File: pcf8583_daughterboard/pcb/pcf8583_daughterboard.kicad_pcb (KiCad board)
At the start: 2 copper layers, 22.9 x 20.3 mm, 11 parts

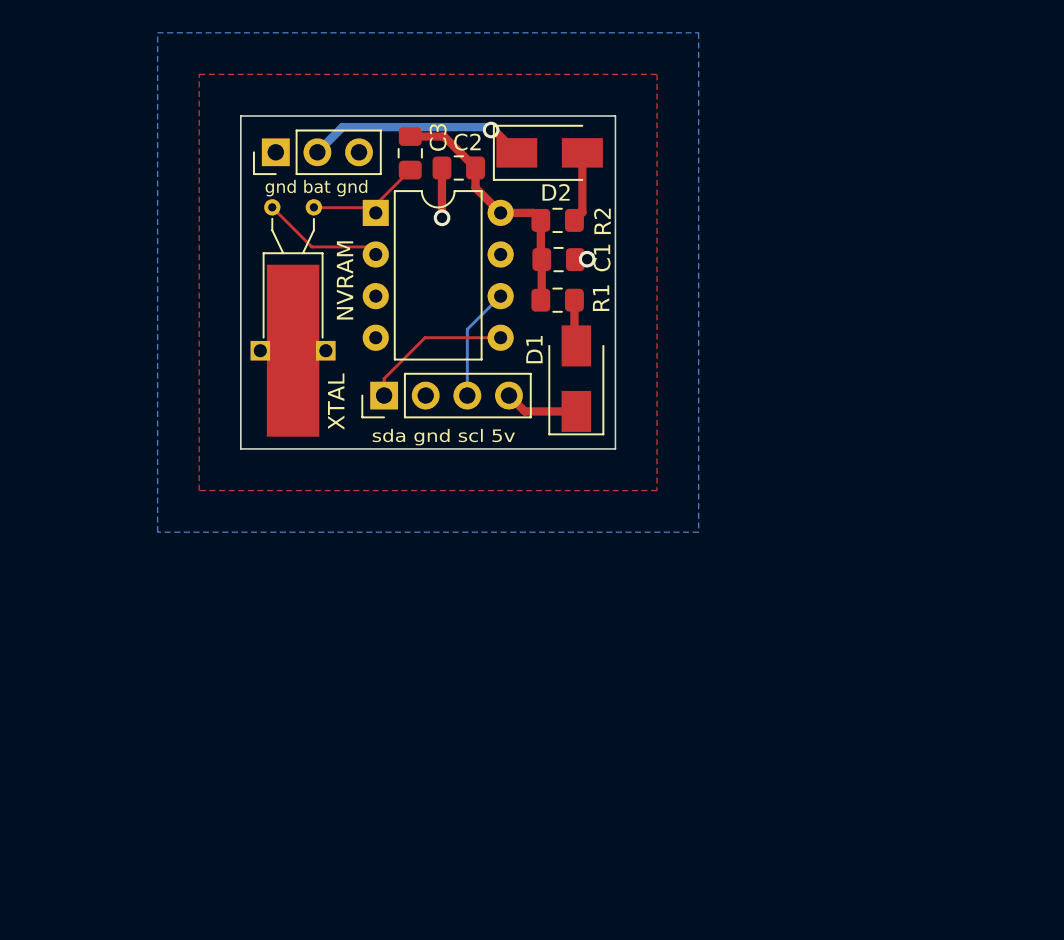
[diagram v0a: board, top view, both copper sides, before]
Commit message: Add supercap to pcf8583 daughterboard and make it a bit bigger, with mounting holes
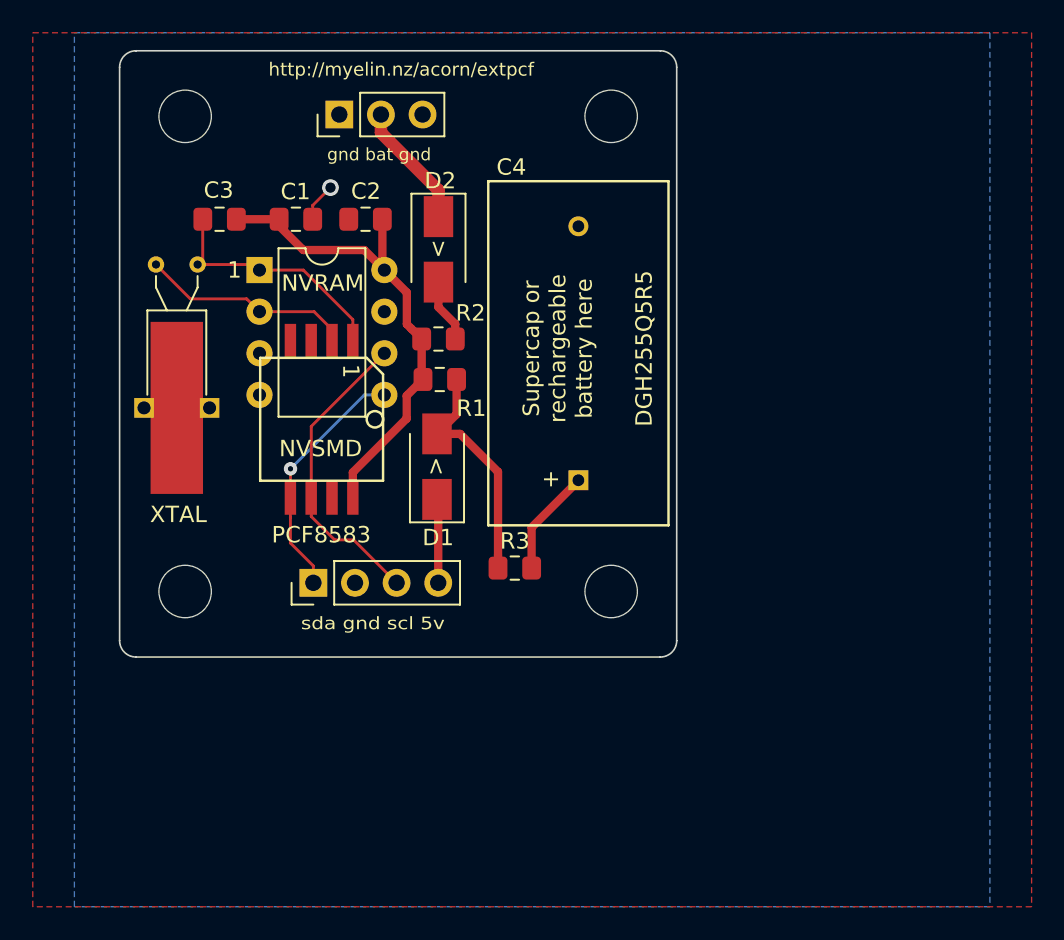
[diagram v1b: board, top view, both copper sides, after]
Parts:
- added C4: DGH255Q5R5, myelin-kicad:dgh255q5r5, F.Cu at (173.0, 108.5)
- added NVSMD: PCF8583, myelin-kicad:so8_pcf8583t_7.5x7.5mm, F.Cu at (157.3, 112.5)
- added R3: 180R, Resistor_SMD:R_0805_2012Metric_Pad1.15x1.40mm_HandSolder, F.Cu at (169.1, 121.6)
- added REF**: MountingHole_3.2mm_M3, MountingHole:MountingHole_3.2mm_M3, F.Cu at (149.0, 94.0)
- added REF**: MountingHole_3.2mm_M3, MountingHole:MountingHole_3.2mm_M3, F.Cu at (175.0, 94.0)
- added REF**: MountingHole_3.2mm_M3, MountingHole:MountingHole_3.2mm_M3, F.Cu at (175.0, 123.0)
- added REF**: MountingHole_3.2mm_M3, MountingHole:MountingHole_3.2mm_M3, F.Cu at (149.0, 123.0)
- NVRAM: value PCF8583P -> PCF8583
- R1, R2: value 100R -> 47R
- moved C1 16.2 mm to (155.8, 100.3)
- moved C3 12.3 mm to (151.1, 100.3), turned to 0 degrees
- moved HDR 12.2 mm to (156.8, 122.5)
- moved R2 10.3 mm to (164.5, 107.6)
- moved D1 10.1 mm to (164.4, 115.4)
- moved D2 8.98 mm to (164.5, 102.1), turned to 270 degrees
- moved R1 8.67 mm to (164.5, 110.1)
- moved NVRAM 7.91 mm to (153.5, 103.4)
- moved XTAL 7.91 mm to (147.2, 103.0)
- moved C2 6.49 mm to (160.0, 100.3)
- moved BATT 4.51 mm to (158.4, 93.9)
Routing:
- net NVR_POWER: track 15.7 -> 30.4 mm
- net SCL: track 6.91 -> 18.7 mm
- net 5VD_cat: track 2.84 -> 14.4 mm
- net OSCI: track 7.40 -> 15.1 mm
- net supercap_P: track 0.00 -> 6.54 mm
- net SDA: track 9.18 -> 15.1 mm, vias 0 -> 1
- net BATT: track 13.5 -> 7.68 mm, vias 1 -> 0
- net OSCO: track 7.51 -> 13.1 mm
- net GND: track 7.78 -> 6.38 mm, vias 2 -> 1
- net 5V: track 4.51 -> 5.12 mm
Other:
- board size 22.9 x 20.3 mm -> 34 x 37 mm
- board text added: "+"
- board text added: "1"
- board text added: ">"
- board text added: "Supercap or rechargeable battery here"
- board text added: "http://myelin.nz/acorn/extpcf Designed by Phillip Pearson Copyright 2019 Google LLC"

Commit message: v2 sent to JLC 5/15
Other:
- board text added: "v2"
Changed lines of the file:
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@@
   (general
     (thickness 1.6)
-    (drawings 18)
+    (drawings 19)
     (tracks 67)
     (zones 0)
@@
       (net 3 NVR_POWER))
   )
+  (gr_text v2 (at 168.41 93.34) (layer F.SilkS)
+    (effects (font (size 1 1) (thickness 0.2)))
+  )
   (gr_text 1 (at 152.01 103.38) (layer F.SilkS)
